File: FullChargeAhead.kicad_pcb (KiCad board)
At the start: 2 copper layers, 38.6 x 25.8 mm, 18 parts, among them P101 CONN_01X02, P102 JST 2 Pin, U101 MCP73834-FCI/UN

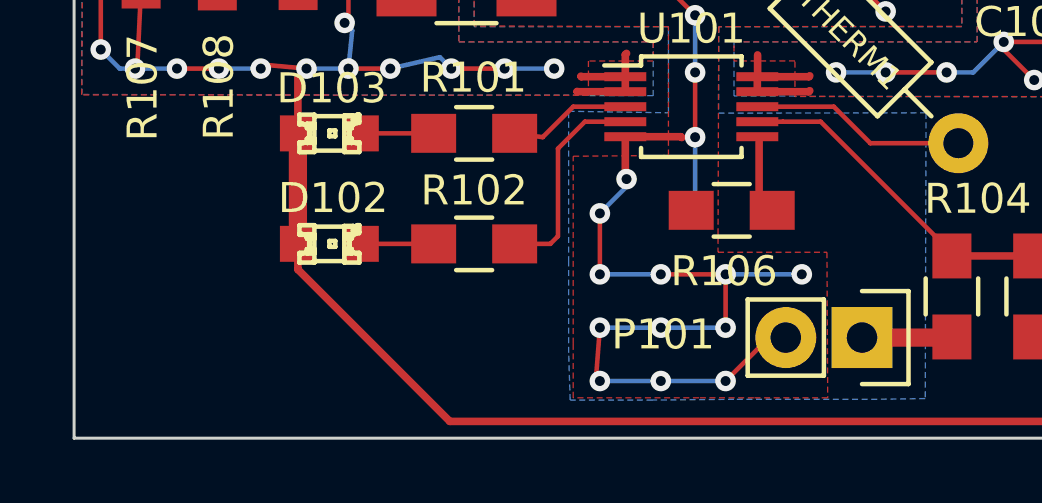
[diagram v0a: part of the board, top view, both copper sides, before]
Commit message: Completed layout and archive for Oshpark
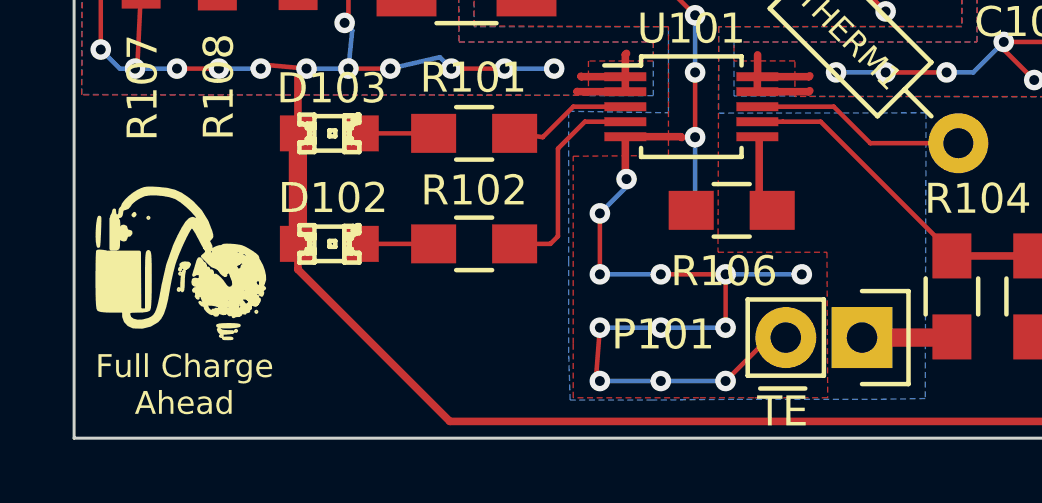
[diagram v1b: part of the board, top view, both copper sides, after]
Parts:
- added G***: LOGO, fca-lib:Full_Charge_Ahead_Icon_6, F.Cu at (90.7, 78.9)
- added G***: LOGO, fca-lib:kicad_logo, B.Cu at (108.6, 60.8)
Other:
- board text added: "Batt"
- board text added: "Full Charge Ahead"
- board text added: "~TE"

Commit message: Final layout and oshpark review
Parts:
- moved G*** 2.68 mm to (106.3, 62.2)

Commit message: The last final layout and shpark review
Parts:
- moved R106 0.35 mm to (108.7, 77.3)
- moved C101 0.13 mm to (100.2, 69.8)
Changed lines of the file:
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@@
     (links 36)
     (no_connects 0)
-    (area 87.071999 59.004999 125.780001 84.886001)
+    (area 83.846057 55.8627 125.780001 84.886001)
     (thickness 1.6)
     (drawings 7)
@@
   )
   (module Capacitors_SMD:C_1206_HandSoldering (layer F.Cu)
-    (at 100.203 69.977)
+    (at 100.203 69.85)
     (descr "Capacitor SMD 1206, hand soldering")
     (tags "capacitor 1206")
@@
   )
   (module Resistors_SMD:R_0805_HandSoldering (layer F.Cu)
-    (at 109.0422 77.2414)
+    (at 108.712 77.343)
     (descr "Resistor SMD 0805, hand soldering")
     (tags "resistor 0805")
